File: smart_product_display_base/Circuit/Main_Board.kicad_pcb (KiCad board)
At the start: 2 copper layers, 42 parts, among them Q1 BD681, Q2 BD681, Q3 BD681, Q4 BD681, Q5 BD681, Q6 BD681, U1 PC817, U2 PC817, U3 PC817, U4 PC817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

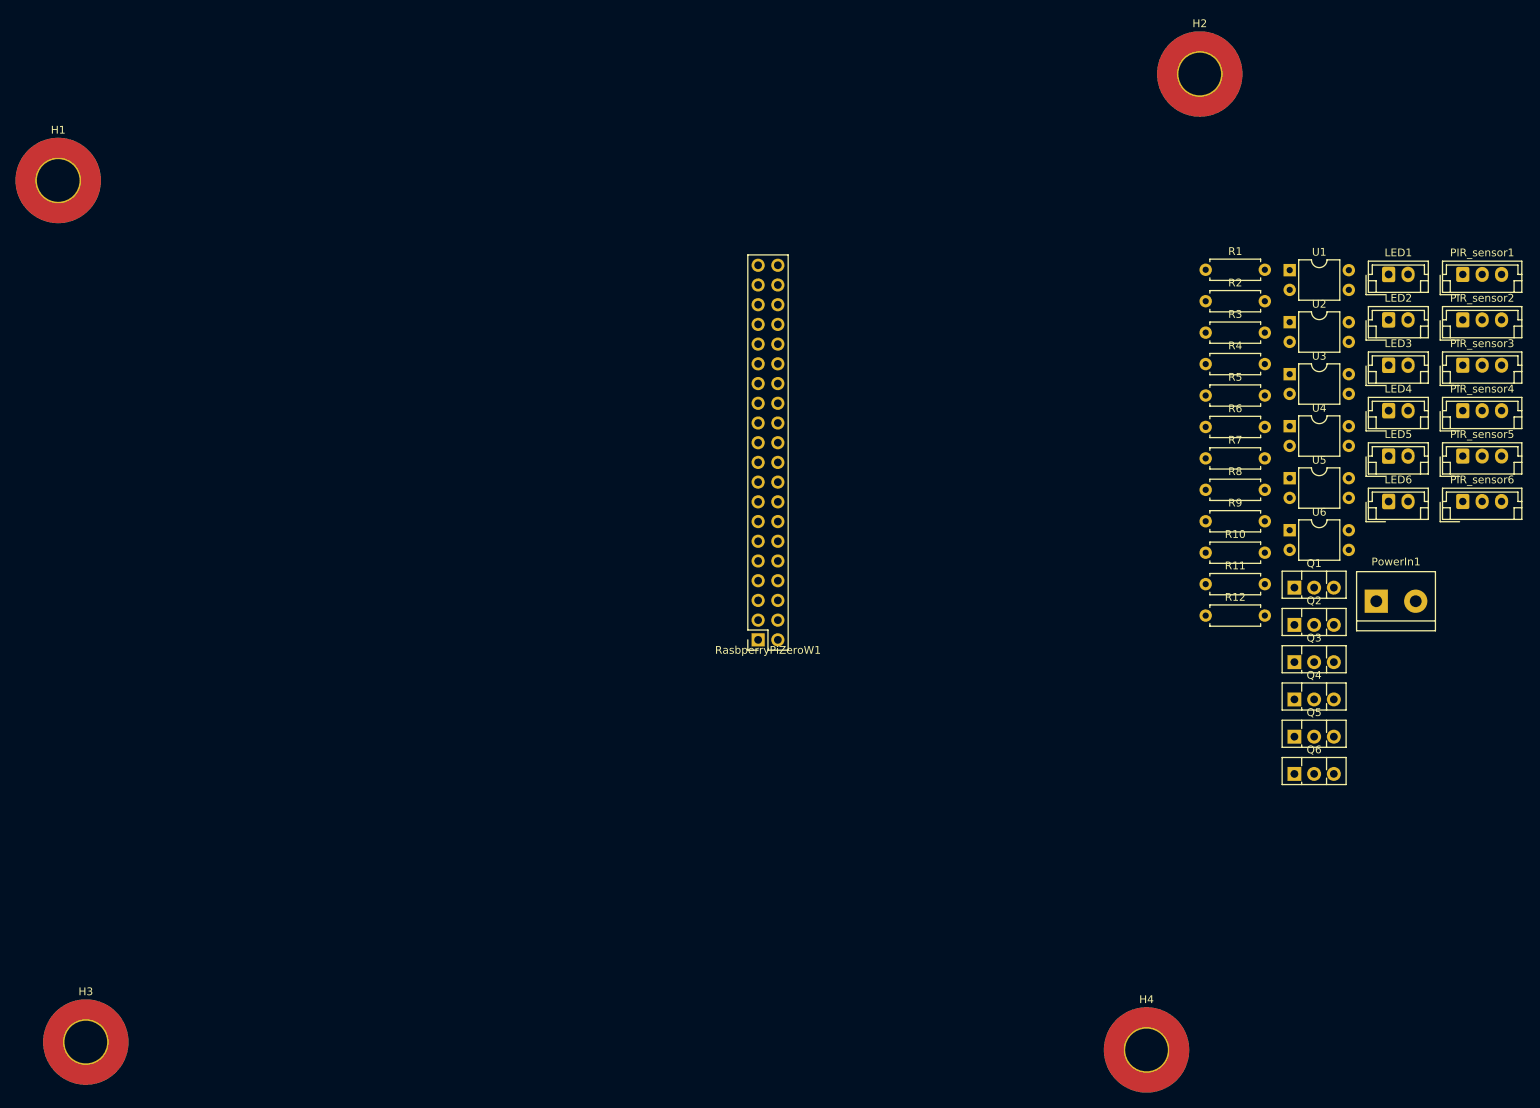
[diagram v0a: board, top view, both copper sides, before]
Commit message: tested Power circuit and finished most PCB layout
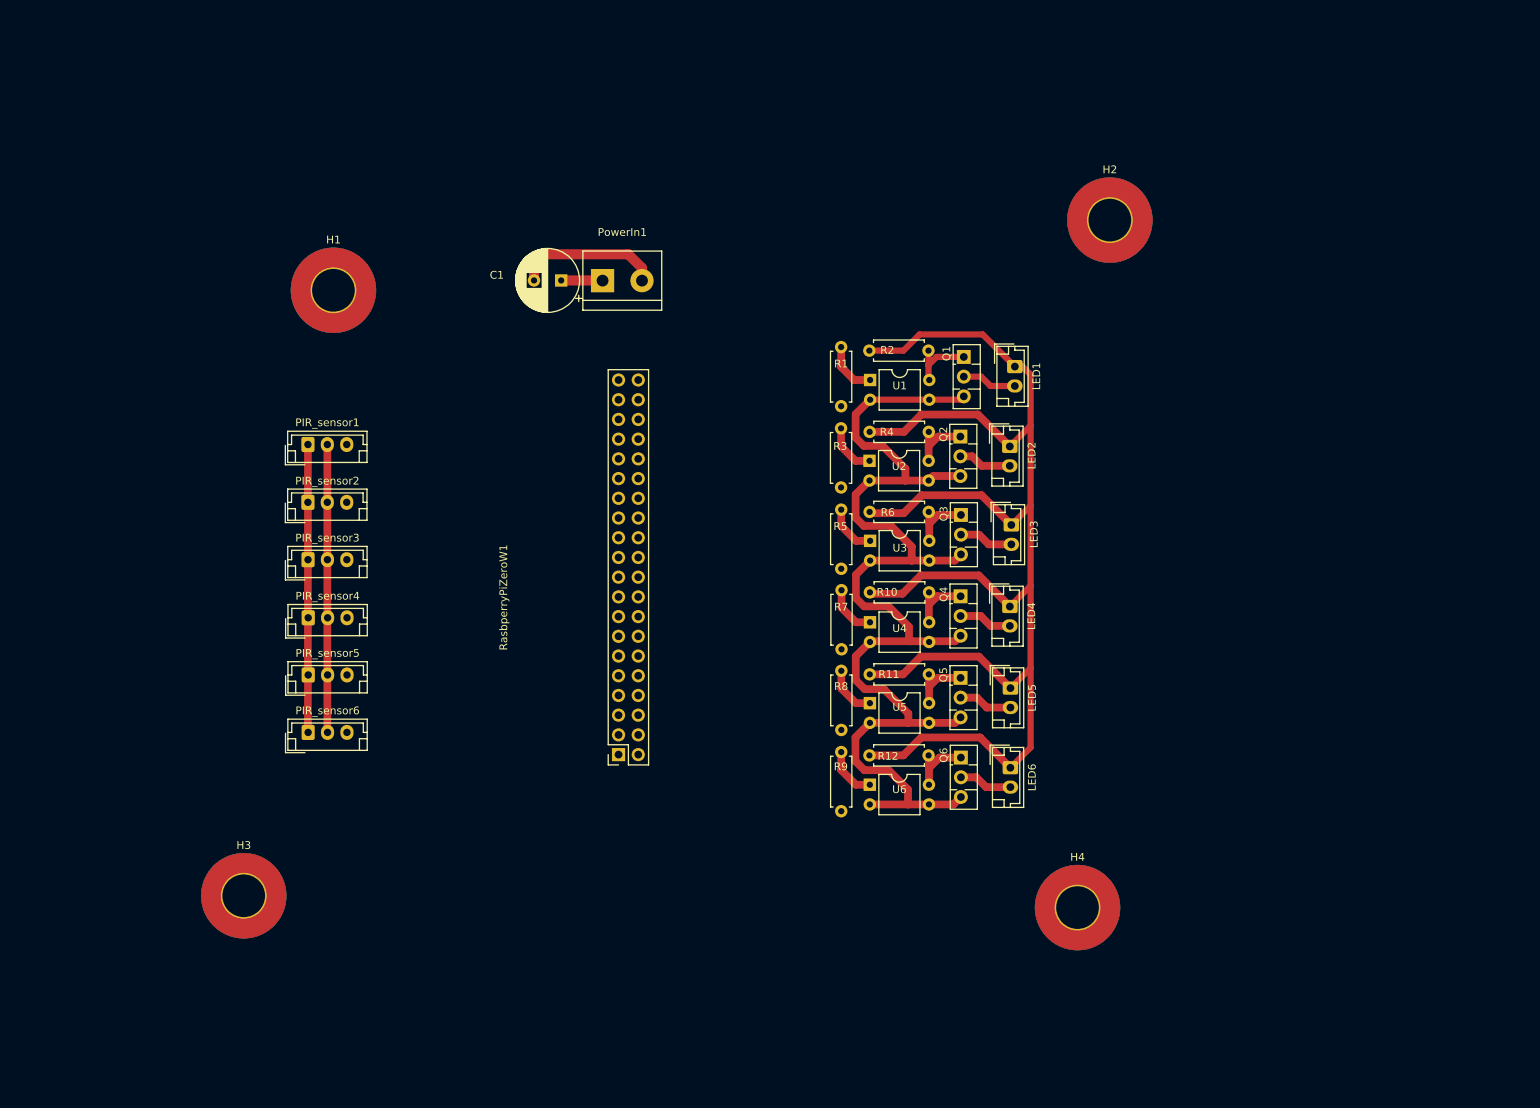
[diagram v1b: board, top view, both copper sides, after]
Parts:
- added C1: 470uF, Capacitor_THT:CP_Radial_D8.0mm_P3.50mm, F.Cu at (125.2, 61.4)
- moved PIR_sensor6 151.7 mm to (92.6, 119.6)
- moved PIR_sensor5 151.4 mm to (92.7, 112.2)
- moved PIR_sensor4 151.1 mm to (92.7, 104.9)
- moved PIR_sensor3 150.9 mm to (92.6, 97.4)
- moved PIR_sensor2 150.6 mm to (92.6, 90.0)
- moved PIR_sensor1 150.4 mm to (92.6, 82.5)
- moved PowerIn1 107.9 mm to (130.6, 61.4)
- moved U6 63.3 mm to (165.0, 126.4)
- moved U5 61.4 mm to (165.0, 115.8)
- moved R9 60.0 mm to (161.3, 129.8), turned to 90 degrees
- moved U4 59.7 mm to (165.0, 105.4)
- moved LED6 59.6 mm to (183.1, 124.2), turned to -90 degrees
- moved U3 58.2 mm to (165.0, 94.9)
- moved LED5 57.2 mm to (183.1, 113.9), turned to -90 degrees
- moved U2 57.0 mm to (165.0, 84.6)
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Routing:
- net +5V: track 0.00 -> 236.4 mm
- net GND: track 0.00 -> 206.6 mm
- net Net-(Q1-B): track 0.00 -> 8.81 mm
- net Net-(Q4-B): track 0.00 -> 8.48 mm
- net Net-(Q6-B): track 0.00 -> 8.47 mm
- net Net-(Q2-B): track 0.00 -> 8.32 mm
- net Net-(Q3-B): track 0.00 -> 8.31 mm
- net Net-(Q5-B): track 0.00 -> 8.25 mm
- net Net-(LED1-Pin_2): track 0.00 -> 7.07 mm
- net Net-(LED3-Pin_2): track 0.00 -> 7.01 mm
- net Net-(R1-Pad2): track 0.00 -> 6.99 mm
- net Net-(LED5-Pin_2): track 0.00 -> 6.95 mm
- net Net-(LED6-Pin_2): track 0.00 -> 6.90 mm
- net Net-(LED4-Pin_2): track 0.00 -> 6.87 mm
- net Net-(LED2-Pin_2): track 0.00 -> 6.87 mm
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
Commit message: finished PCB layout
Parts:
- removed H1, H4: MountingHole, MountingHole:MountingHole_5.5mm_Pad_TopBottom
- removed LED5, LED6: JST-2p, Connector_JST:JST_EH_B2B-EH-A_1x02_P2.50mm_Vertical
- removed PIR_sensor5, PIR_sensor6: JST-3p, Connector_JST:JST_EH_B3B-EH-A_1x03_P2.50mm_Vertical
- removed Q5, Q6: BD681, Package_TO_SOT_THT:TO-126-3_Vertical
- removed RasbperryPiZeroW1: PinHeader2x20, Connector_PinSocket_2.54mm:PinSocket_2x20_P2.54mm_Vertical
- removed U5, U6: PC817, Package_DIP:DIP-4_W7.62mm
- added H5: MountingHole, MountingHole:MountingHole_2.5mm_Pad_TopOnly, F.Cu at (115.7, 75.1)
- added H6: MountingHole, MountingHole:MountingHole_2.5mm_Pad_TopOnly, F.Cu at (115.7, 133.1)
- added R13: 10k, Resistor_THT:R_Axial_DIN0207_L6.3mm_D2.5mm_P7.62mm_Horizontal, F.Cu at (160.1, 115.4)
- added R14: 20k, Resistor_THT:R_Axial_DIN0207_L6.3mm_D2.5mm_P7.62mm_Horizontal, F.Cu at (163.1, 123.0)
- added R15: 10k, Resistor_THT:R_Axial_DIN0207_L6.3mm_D2.5mm_P7.62mm_Horizontal, F.Cu at (167.7, 115.4)
- added R16: 20k, Resistor_THT:R_Axial_DIN0207_L6.3mm_D2.5mm_P7.62mm_Horizontal, F.Cu at (170.7, 123.0)
- added RaspberryPiZeroW1: Conn_02x20, Connector_PinSocket_2.54mm:PinSocket_2x20_P2.54mm_Vertical, F.Cu at (140.0, 80.0)
- H2, H3: footprint MountingHole:MountingHole_5.5mm_Pad_TopBottom -> MountingHole:MountingHole_4mm_Pad_TopOnly
- R11: value 1k -> 10k
- R12: value 1k -> 20k
- R8: value 330 -> 10k
- R9: value 330 -> 20k
- moved H3 113.1 mm to (168.1, 64.7)
- moved PIR_sensor4 81.3 mm to (168.9, 133.2), turned to 90 degrees
- moved H2 80.1 mm to (116.7, 65.3)
- moved PIR_sensor3 77.5 mm to (161.4, 133.2), turned to 90 degrees
- moved PIR_sensor2 75.1 mm to (154.0, 133.2), turned to 90 degrees
- moved PIR_sensor1 74.0 mm to (146.6, 133.2), turned to 90 degrees
- moved C1 30.9 mm to (156.0, 64.9), turned to 0 degrees
- moved R11 20.3 mm to (152.6, 115.5), turned to -90 degrees
- moved PowerIn1 20.2 mm to (150.4, 65.3), turned to 180 degrees
- moved R12 17.0 mm to (155.6, 123.1), turned to 90 degrees
- moved R8 16.5 mm to (145.3, 115.5), turned to -90 degrees
- moved R9 14.6 mm to (148.3, 123.1)
- moved LED1 14.2 mm to (169.8, 75.4)
- moved LED2 14.2 mm to (169.2, 85.7)
- moved LED3 14.2 mm to (169.4, 95.8)
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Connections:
- PIR_sensor1 pad 1: GND -> +5V
- PIR_sensor1 pad 2: +5V -> GND
- PIR_sensor1 pad 3: PIR1_signal -> Net-(PIR_sensor1-Pin_3)
- PIR_sensor2 pad 1: GND -> +5V
- PIR_sensor2 pad 2: +5V -> GND
- PIR_sensor2 pad 3: PIR2_signal -> Net-(PIR_sensor2-Pin_3)
- PIR_sensor3 pad 1: GND -> +5V
- PIR_sensor3 pad 2: +5V -> GND
- PIR_sensor3 pad 3: PIR3_signal -> Net-(PIR_sensor3-Pin_3)
- PIR_sensor4 pad 1: GND -> +5V
- PIR_sensor4 pad 2: +5V -> GND
- PIR_sensor4 pad 3: PIR4_signal -> Net-(PIR_sensor4-Pin_3)
- R11 pad 1: Net-(Q5-B) -> PIR2_signal
- R11 pad 2: +5V -> Net-(PIR_sensor2-Pin_3)
- R12 pad 1: Net-(Q6-B) -> GND
- R12 pad 2: +5V -> PIR2_signal
- R8 pad 1: LED5_control -> PIR1_signal
- R8 pad 2: Net-(R8-Pad2) -> Net-(PIR_sensor1-Pin_3)
- R9 pad 1: LED6_control -> GND
- R9 pad 2: Net-(R9-Pad2) -> PIR1_signal
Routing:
- net GND: track 206.6 -> 294.6 mm
- net PIR4_signal: track 0.00 -> 38.4 mm
- net PIR3_signal: track 0.00 -> 28.0 mm
- net PIR2_signal: track 0.00 -> 20.4 mm
- net LED1_control: track 0.00 -> 16.8 mm
- net LED2_control: track 0.00 -> 12.2 mm
- net +5V: track 236.4 -> 224.3 mm
- net PIR1_signal: track 0.00 -> 11.2 mm
- net LED4_control: track 0.00 -> 9.14 mm
- net Net-(Q6-B): track 8.47 -> 0.00 mm
- net Net-(Q5-B): track 8.25 -> 0.00 mm
- net LED3_control: track 0.00 -> 7.96 mm
- net Net-(LED5-Pin_2): track 6.95 -> 0.00 mm
- net Net-(LED6-Pin_2): track 6.90 -> 0.00 mm
- net Net-(R9-Pad2): track 6.79 -> 0.00 mm
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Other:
- board outline added: 63.9 x 77.9 mm
- board text added: "Smart Product Display"
